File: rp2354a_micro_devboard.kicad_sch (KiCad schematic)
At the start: 52 parts, among them J1 USB_C_Receptacle_USB2.0_16P, J2 01x20_PinHeader_P2.54mm, J3 01x20_PinHeader_P2.54mm, J4 SWD_XH_3p, SW1 SW_SPST, SW2 SW_SPST, U1 TMI3112H, U2 RP2354A, Y1 YIC 12M10PB

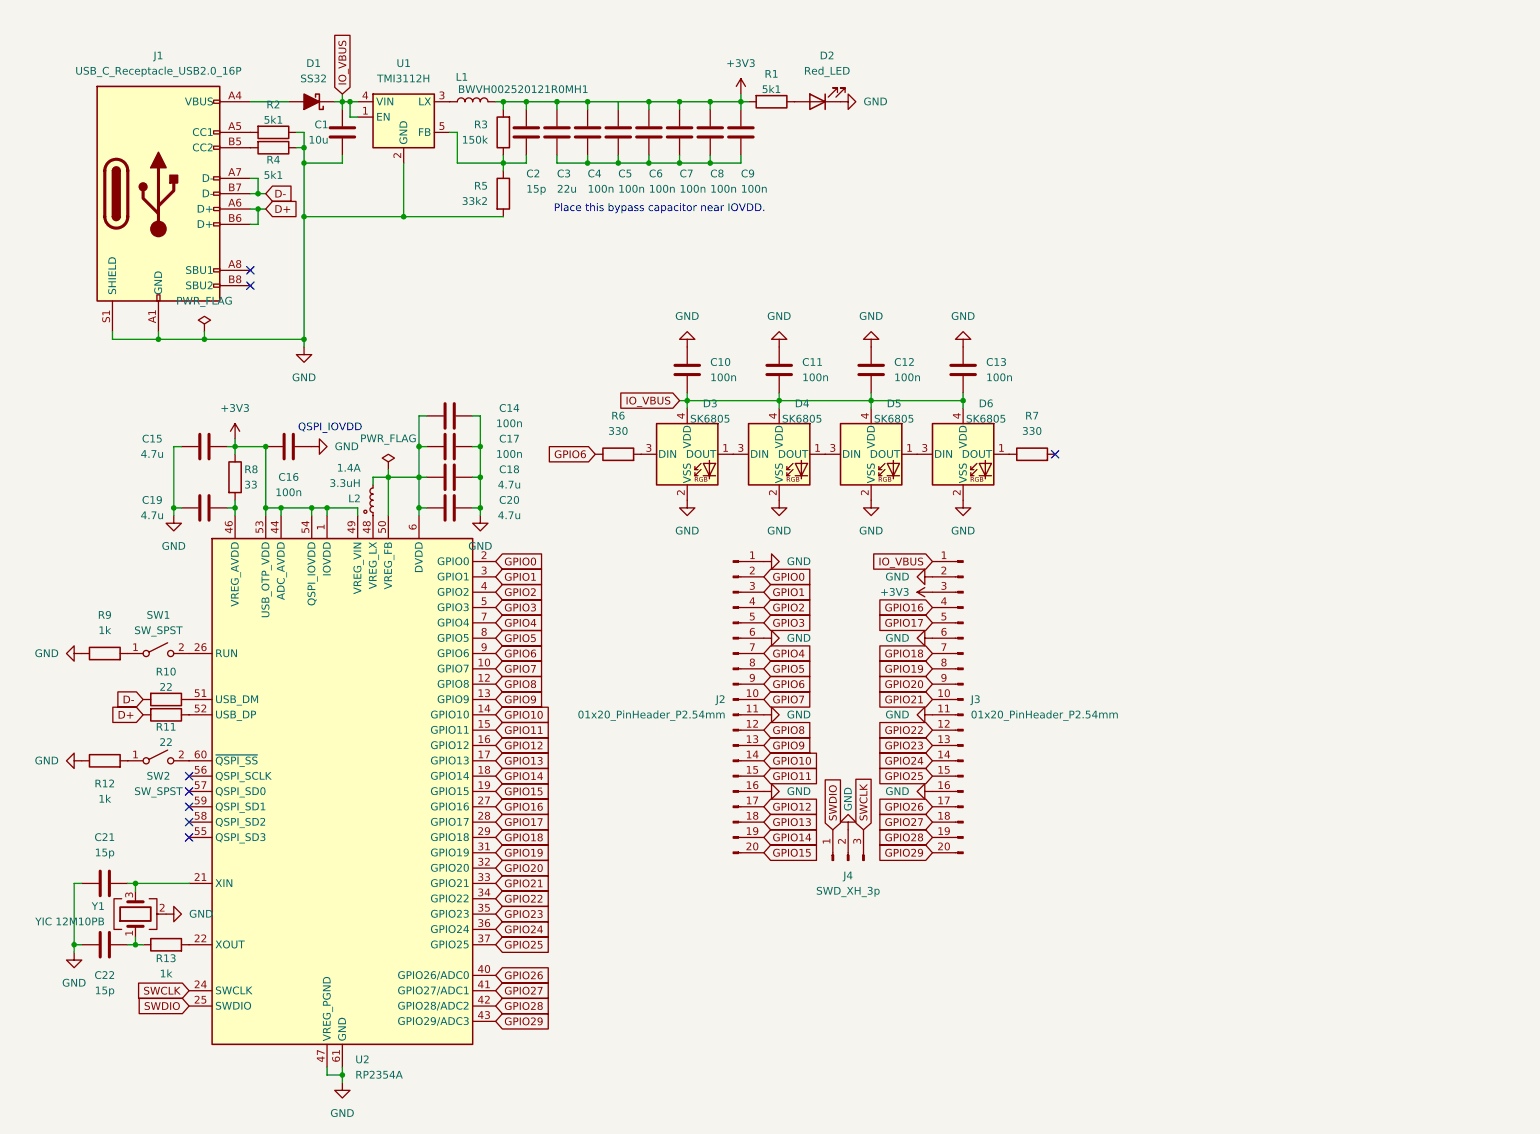
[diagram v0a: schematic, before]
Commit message: feat: add battely charge&source. but kind to 1S-LiPo only.
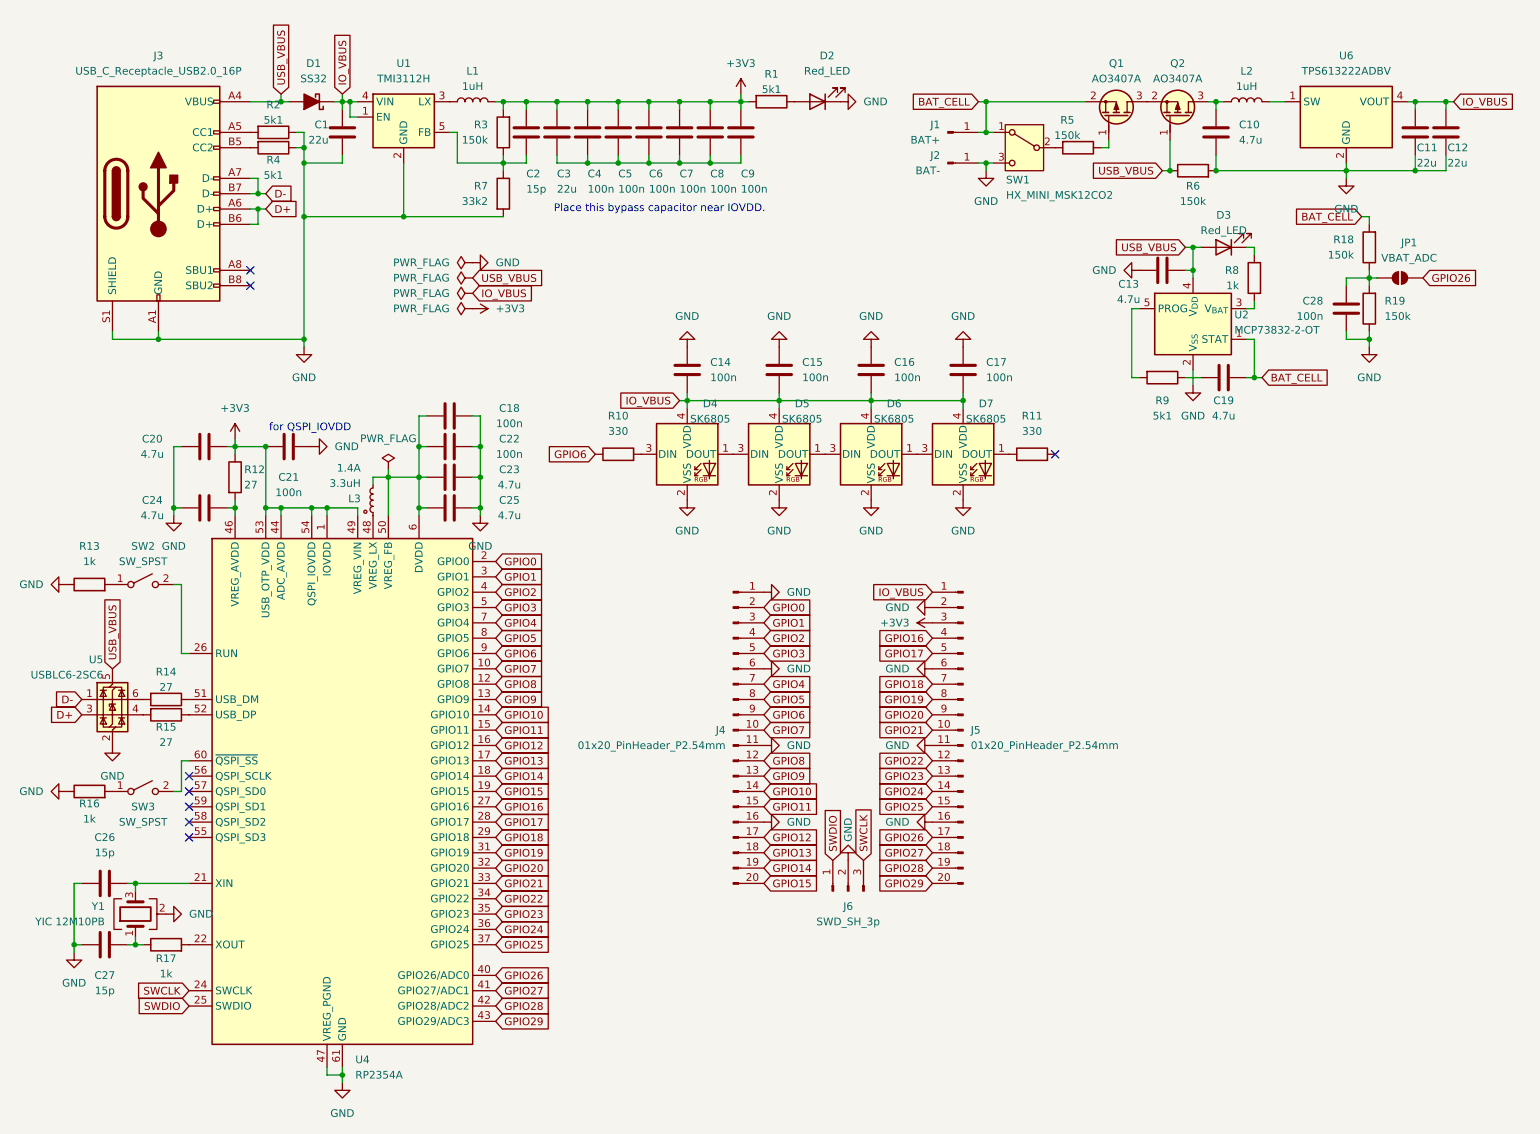
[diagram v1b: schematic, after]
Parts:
- added C10, C13, C19: 4.7u, Capacitor_SMD:C_0603_1608Metric, symbol Device:C
- added C11, C12: 22u, Capacitor_SMD:C_0603_1608Metric, symbol Device:C
- added C28: 100n, Capacitor_SMD:C_0402_1005Metric, symbol Device:C
- added D3: Red_LED, LED_SMD:LED_0603_1608Metric, symbol Device:LED
- added J1: BAT+, Connector_Wire:SolderWirePad_1x01_SMD_1x2mm, symbol Connector:Conn_01x01_Pin
- added J2: BAT-, Connector_Wire:SolderWirePad_1x01_SMD_1x2mm, symbol Connector:Conn_01x01_Pin
- added JP1: VBAT_ADC, Jumper:SolderJumper-2_P1.3mm_Open_Pad1.0x1.5mm, symbol Jumper:SolderJumper_2_Open
- added L2: 1uH, Inductor_SMD:L_1008_2520Metric, symbol Device:L
- added Q1, Q2: AO3407A, PCM_Package_TO_SOT_SMD_AKL:SOT-23, symbol PCM_Transistor_MOSFET_AKL:AO3407A
- added R18, R19, R5, R6: 150k, Resistor_SMD:R_0402_1005Metric, symbol Device:R
- added R8: 1k, Resistor_SMD:R_0402_1005Metric, symbol Device:R
- added R9: 5k1, Resistor_SMD:R_0402_1005Metric, symbol Device:R
- added SW1: HX_MINI_MSK12CO2, Download_Lib:HX_MINI_MSK12CO2, symbol Switch:SW_SPDT
- added U2: MCP73832-2-OT, Package_TO_SOT_SMD:SOT-23-5, symbol Battery_Management:MCP73832-2-OT
- added U5: USBLC6-2SC6, Package_TO_SOT_SMD:SOT-23-6, symbol Power_Protection:USBLC6-2SC6
- added U6: TPS613222ADBV, Package_TO_SOT_SMD:SOT-23-5, symbol Regulator_Switching:TPS613222ADBV
- C1: value 10u -> 22u
- C2: footprint Capacitor_SMD:C_0603_1608Metric -> Capacitor_SMD:C_0402_1005Metric
- C26: renamed from C21; footprint Capacitor_SMD:C_0603_1608Metric -> Capacitor_SMD:C_0402_1005Metric
- C27: renamed from C22; footprint Capacitor_SMD:C_0603_1608Metric -> Capacitor_SMD:C_0402_1005Metric
- J6: renamed from J4; value SWD_XH_3p -> SWD_SH_3p; footprint Connector_JST:JST_XH_B3B-XH-A_1x03_P2.50mm_Vertical -> Connector_JST:JST_SH_BM03B-SRSS-TB_1x03-1MP_P1.00mm_Vertical
- L1: value BWVH002520121R0MH1 -> 1uH
- R1, R2, R3, R4: footprint Resistor_SMD:R_0603_1608Metric -> Resistor_SMD:R_0402_1005Metric
- R10: renamed from R6; footprint Resistor_SMD:R_0603_1608Metric -> Resistor_SMD:R_0402_1005Metric
- R11: renamed from R7; footprint Resistor_SMD:R_0603_1608Metric -> Resistor_SMD:R_0402_1005Metric
- R12: renamed from R8; value 33 -> 27; footprint Resistor_SMD:R_0603_1608Metric -> Resistor_SMD:R_0402_1005Metric
- R13: renamed from R9; footprint Resistor_SMD:R_0603_1608Metric -> Resistor_SMD:R_0402_1005Metric
- R14: renamed from R10; value 22 -> 27; footprint Resistor_SMD:R_0603_1608Metric -> Resistor_SMD:R_0402_1005Metric
- R15: renamed from R11; value 22 -> 27; footprint Resistor_SMD:R_0603_1608Metric -> Resistor_SMD:R_0402_1005Metric
- R16: renamed from R12; footprint Resistor_SMD:R_0603_1608Metric -> Resistor_SMD:R_0402_1005Metric
- R17: renamed from R13; footprint Resistor_SMD:R_0603_1608Metric -> Resistor_SMD:R_0402_1005Metric
- R7: renamed from R5; footprint Resistor_SMD:R_0603_1608Metric -> Resistor_SMD:R_0402_1005Metric
- renumbered C10 to C14, C11 to C15, C12 to C16, C13 to C17, C14 to C18, C15 to C20, C16 to C21, C17 to C22, C18 to C23, C19 to C24, C20 to C25, D3 to D4, D4 to D5, D5 to D6, D6 to D7, J1 to J3, J2 to J4, J3 to J5, L2 to L3, SW1 to SW2, SW2 to SW3, U2 to U4
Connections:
- net +3V3: now also C5.1
- net D+: now also U5.3 (I/O2); no longer R15.2
- net D-: now also U5.1 (I/O1); no longer R14.2
- net GND: now also C10.2, C11.2, C12.2, C13.1, C28.2, J2.1 (Pin_1), R19.1, R6.2, SW1.3 (C), U2.2 (V_{SS}), U5.2 (GND), U6.2 (GND)
- net GPIO26: now also JP1.2 (B)
- net IO_VBUS: now also C11.1, C12.1, U6.4 (VOUT)
- net USB_VBUS: now reaches D1.2 (A), J3.A4 (VBUS), J3.A9 (VBUS), J3.B4 (VBUS), J3.B9 (VBUS)
- net USB_VBUS: now also C13.2, D3.2 (A), Q2.1 (G), R6.1, U2.4 (V_{DD}), U5.5 (VBUS)
- new net: R5.2, SW1.2 (B)
- new net: Q1.1 (G), R5.1
- new net: D3.1 (K), R8.1
- new net: R8.2, U2.3 (V_{BAT})
- new net: R9.2, U2.5 (PROG)
- new net: C28.1, JP1.1 (A), R18.1, R19.2
- new net: Q1.3 (D), Q2.2 (S)
- new net: C10.1, L2.1, Q2.3 (D)
- new net: R15.2, U5.4 (I/O2)
- new net: L2.2, U6.1 (SW)
- new net: C19.2, R9.1
- new net: R14.2, U5.6 (I/O1)
- new net BAT_CELL: C19.1, J1.1 (Pin_1), Q1.2 (S), R18.2, SW1.1 (A), U2.1 (STAT)
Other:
- note added: "for QSPI_IOVDD"
- note removed: "QSPI_IOVDD"
- company: (none) -> EsEhEhElp
- title: (none) -> RP2354A_Micro_Devboard
- moved on the sheet: J4, J5, J6, R13, R16, SW2, SW3
